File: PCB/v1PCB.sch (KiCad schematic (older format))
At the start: 218 parts, among them SW1 SW_PUSH, SW2 SW_PUSH, U1 STM32F072CBUx, U2 MCP1700-3302E_SOT23

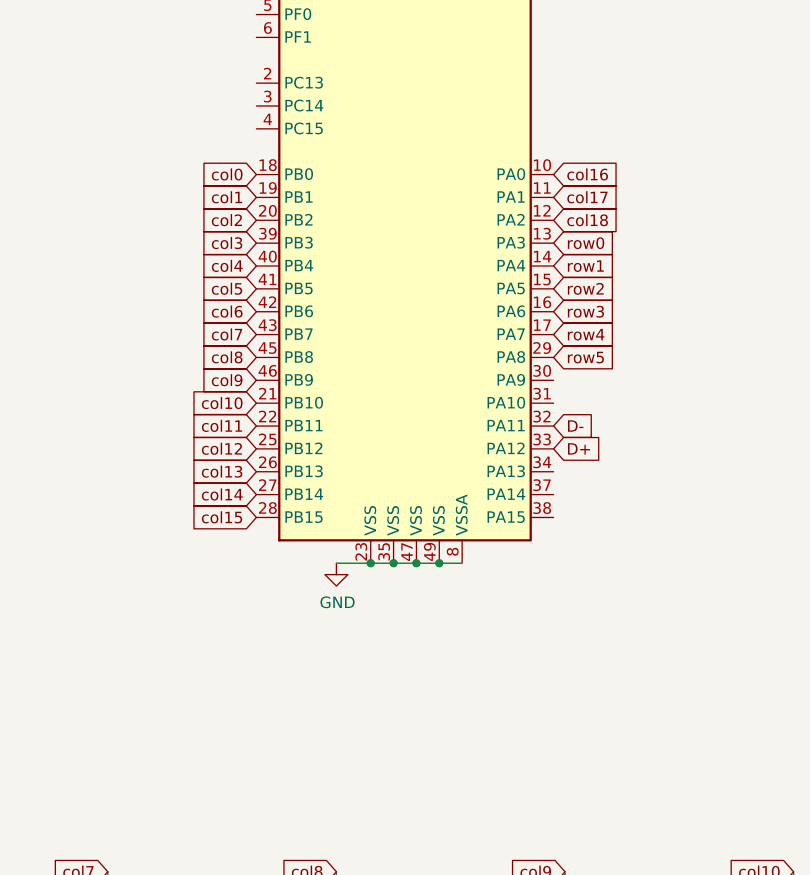
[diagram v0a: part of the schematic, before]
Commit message: Fixed a few runs, still need to add USB and redo VDDIO decoupling capacitors
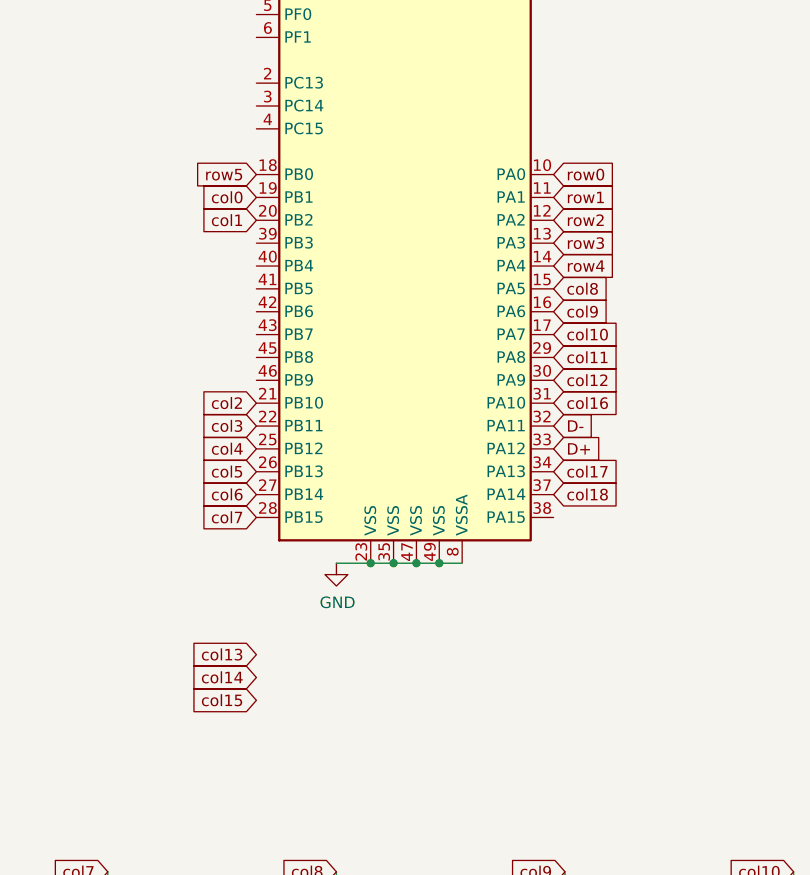
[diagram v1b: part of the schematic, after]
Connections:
- net col0: now also U1.19 (PB1); no longer U1.18 (PB0)
- net col1: now also U1.20 (PB2); no longer U1.19 (PB1)
- net col10: now also U1.17 (PA7); no longer U1.21 (PB10)
- net col11: now also U1.29 (PA8); no longer U1.22 (PB11)
- net col12: now also U1.30 (PA9); no longer U1.25 (PB12)
- net col13: no longer U1.26 (PB13)
- net col14: no longer U1.27 (PB14)
- net col15: no longer U1.28 (PB15)
- net col16: now also U1.31 (PA10); no longer U1.10 (PA0)
- net col17: now also U1.34 (PA13); no longer U1.11 (PA1)
- net col18: now also U1.37 (PA14); no longer U1.12 (PA2)
- net col2: now also U1.21 (PB10); no longer U1.20 (PB2)
- net col3: now also U1.22 (PB11); no longer U1.39 (PB3)
- net col4: now also U1.25 (PB12); no longer U1.40 (PB4)
- net col5: now also U1.26 (PB13); no longer U1.41 (PB5)
- net col6: now also U1.27 (PB14); no longer U1.42 (PB6)
- net col7: now also U1.28 (PB15); no longer U1.43 (PB7)
- net col8: now also U1.15 (PA5); no longer U1.45 (PB8)
- net col9: now also U1.16 (PA6); no longer U1.46 (PB9)
- net row0: now also U1.10 (PA0); no longer U1.13 (PA3)
- net row1: now also U1.11 (PA1); no longer U1.14 (PA4)
- net row2: now also U1.12 (PA2); no longer U1.15 (PA5)
- net row3: now also U1.13 (PA3); no longer U1.16 (PA6)
- net row4: now also U1.14 (PA4); no longer U1.17 (PA7)
- net row5: now also U1.18 (PB0); no longer U1.29 (PA8)
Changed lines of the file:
@@
 EESchema Schematic File Version 4
+LIBS:v1PCB-cache
 EELAYER 30 0
 EELAYER END
@@
 	20850 5750 20850 6750
 $Comp
-L MCU_ST_STM32F0:STM32F072CBUx U1
-U 1 1 5F25C889
-P 11200 2600
-F 0 "U1" H 11150 4281 50  0000 C CNN
-F 1 "STM32F072CBUx" H 11150 4190 50  0000 C CNN
-F 2 "Package_DFN_QFN:QFN-48-1EP_7x7mm_P0.5mm_EP5.6x5.6mm" H 10600 1200 50  0001 R CNN
-F 3 "http://www.st.com/st-web-ui/static/active/en/resource/technical/document/datasheet/DM00090510.pdf" H 11200 2600 50  0001 C CNN
-	1    11200 2600
-	1    0    0    -1
-$EndComp
-$Comp
 L Regulator_Linear:MCP1700-3302E_SOT23 U2
 U 1 1 5F2612C5
@@
 Wire Wire Line
 	13950 2000 13950 2150
-Connection ~ 11100 1100
-Connection ~ 11200 1100
-Connection ~ 11300 1100
-Connection ~ 11400 1100
 $Comp
 L power:+3.3V #PWR0104
@@
 Text GLabel 11800 3600 2    50   Input ~ 0
 D+
-Connection ~ 11000 4100
-Wire Wire Line
-	11000 4100 10850 4100
-Connection ~ 11100 4100
-Connection ~ 11200 4100
-Connection ~ 11300 4100
 $Comp
 L Device:R_Small R1
@@
 Wire Wire Line
 	6250 2200 6500 2200
-Wire Wire Line
-	11400 4100 11300 4100
-Wire Wire Line
-	11300 4100 11200 4100
-Wire Wire Line
-	11200 4100 11100 4100
-Wire Wire Line
-	11100 4100 11000 4100
-Wire Wire Line
-	11400 1100 11550 1100
-Wire Wire Line
-	11300 1100 11400 1100
-Wire Wire Line
-	11200 1100 11300 1100
-Wire Wire Line
-	11100 1100 11200 1100
-Wire Wire Line
-	11000 1100 11100 1100
-Text GLabel 11800 2700 2    50   Input ~ 0
-row0
-Text GLabel 11800 2800 2    50   Input ~ 0
-row1
-Text GLabel 11800 2900 2    50   Input ~ 0
-row2
-Text GLabel 11800 3000 2    50   Input ~ 0
-row3
-Text GLabel 11800 3100 2    50   Input ~ 0
-row4
-Text GLabel 11800 3200 2    50   Input ~ 0
-row5
-Text GLabel 10500 2500 0    50   Input ~ 0
-col1
-Text GLabel 10500 2400 0    50   Input ~ 0
-col0
-Text GLabel 10500 2600 0    50   Input ~ 0
-col2
-Text GLabel 10500 2700 0    50   Input ~ 0
-col3
-Text GLabel 10500 2800 0    50   Input ~ 0
-col4
-Text GLabel 10500 2900 0    50   Input ~ 0
-col5
-Text GLabel 10500 3000 0    50   Input ~ 0
-col6
-Text GLabel 10500 3100 0    50   Input ~ 0
-col7
-Text GLabel 10500 3200 0    50   Input ~ 0
-col8
-Text GLabel 10500 3300 0    50   Input ~ 0
-col9
-Text GLabel 10500 3400 0    50   Input ~ 0
-col10
-Text GLabel 10500 3500 0    50   Input ~ 0
-col11
-Text GLabel 10500 3600 0    50   Input ~ 0
-col12
-Text GLabel 10500 3700 0    50   Input ~ 0
-col13
-Text GLabel 10500 3800 0    50   Input ~ 0
-col14
-Text GLabel 10500 3900 0    50   Input ~ 0
-col15
-Text GLabel 11800 2400 2    50   Input ~ 0
+Text GLabel 11800 3400 2    50   Input ~ 0
 col16
-Text GLabel 11800 2500 2    50   Input ~ 0
+Text GLabel 11800 3700 2    50   Input ~ 0
 col17
-Text GLabel 11800 2600 2    50   Input ~ 0
+Text GLabel 11800 3800 2    50   Input ~ 0
 col18
 $Comp
@@
 $EndComp
 Connection ~ 6500 2200
+Text GLabel 11800 2800 2    50   Input ~ 0
+row4
+Text GLabel 11800 2700 2    50   Input ~ 0
+row3
+Text GLabel 11800 2600 2    50   Input ~ 0
+row2
+Text GLabel 11800 2500 2    50   Input ~ 0
+row1
+Text GLabel 11800 2400 2    50   Input ~ 0
+row0
+Text GLabel 10500 3500 0    50   Input ~ 0
+col3
+Text GLabel 10500 3600 0    50   Input ~ 0
+col4
+Text GLabel 10500 3700 0    50   Input ~ 0
+col5
+Text GLabel 10500 3800 0    50   Input ~ 0
+col6
+Text GLabel 10500 3900 0    50   Input ~ 0
+col7
+Text GLabel 11800 3000 2    50   Input ~ 0
+col9
+Text GLabel 11800 3100 2    50   Input ~ 0
+col10
+Text GLabel 11800 3300 2    50   Input ~ 0
+col12
+Text GLabel 10500 4500 0    50   Input ~ 0
+col13
+Text GLabel 10500 4600 0    50   Input ~ 0
+col14
+Text GLabel 10500 4700 0    50   Input ~ 0
+col15
+Text GLabel 10500 3400 0    50   Input ~ 0
+col2
+Connection ~ 11100 1100
+Connection ~ 11200 1100
+Connection ~ 11300 1100
+Connection ~ 11400 1100
+Connection ~ 11000 4100
+Wire Wire Line
+	11000 4100 10850 4100
+Wire Wire Line
+	11100 4100 11000 4100
+Connection ~ 11100 4100
+Connection ~ 11200 4100
+Connection ~ 11300 4100
+Wire Wire Line
+	11000 1100 11100 1100
+Wire Wire Line
+	11400 4100 11300 4100
+Wire Wire Line
+	11300 1100 11400 1100
+Wire Wire Line
+	11300 4100 11200 4100
+Wire Wire Line
+	11200 1100 11300 1100
+Wire Wire Line
+	11200 4100 11100 4100
+Wire Wire Line
+	11100 1100 11200 1100
+Wire Wire Line
+	11400 1100 11550 1100
+Text GLabel 11800 2900 2    50   Input ~ 0
+col8
+$Comp
+L MCU_ST_STM32F0:STM32F072CBUx U1
+U 1 1 5F25C889
+P 11200 2600
+F 0 "U1" H 11150 4281 50  0000 C CNN
+F 1 "STM32F072CBUx" H 11150 4190 50  0000 C CNN
+F 2 "Package_DFN_QFN:QFN-48-1EP_7x7mm_P0.5mm_EP5.6x5.6mm" H 10600 1200 50  0001 R CNN
+F 3 "http://www.st.com/st-web-ui/static/active/en/resource/technical/document/datasheet/DM00090510.pdf" H 11200 2600 50  0001 C CNN
+	1    11200 2600
+	1    0    0    -1
+$EndComp
+Text GLabel 11800 3200 2    50   Input ~ 0
+col11
+Text GLabel 10500 2500 0    50   Input ~ 0
+col0
+Text GLabel 10500 2600 0    50   Input ~ 0
+col1
+Text GLabel 10500 2400 0    50   Input ~ 0
+row5
 $EndSCHEMATC

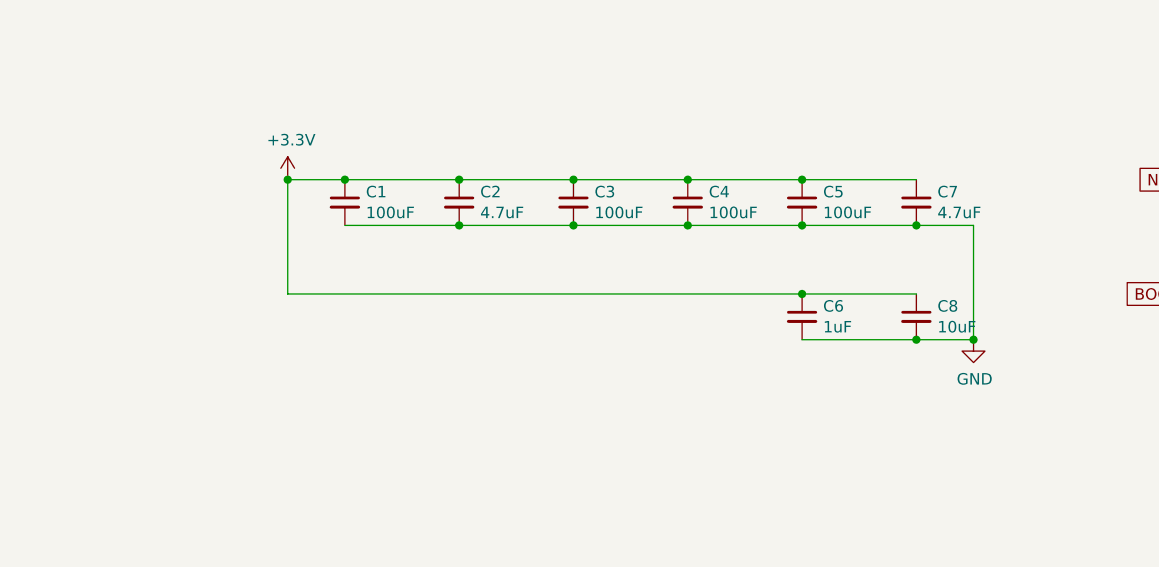
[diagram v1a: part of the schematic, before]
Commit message: Almost done with cap placement, still neeed to add USBC
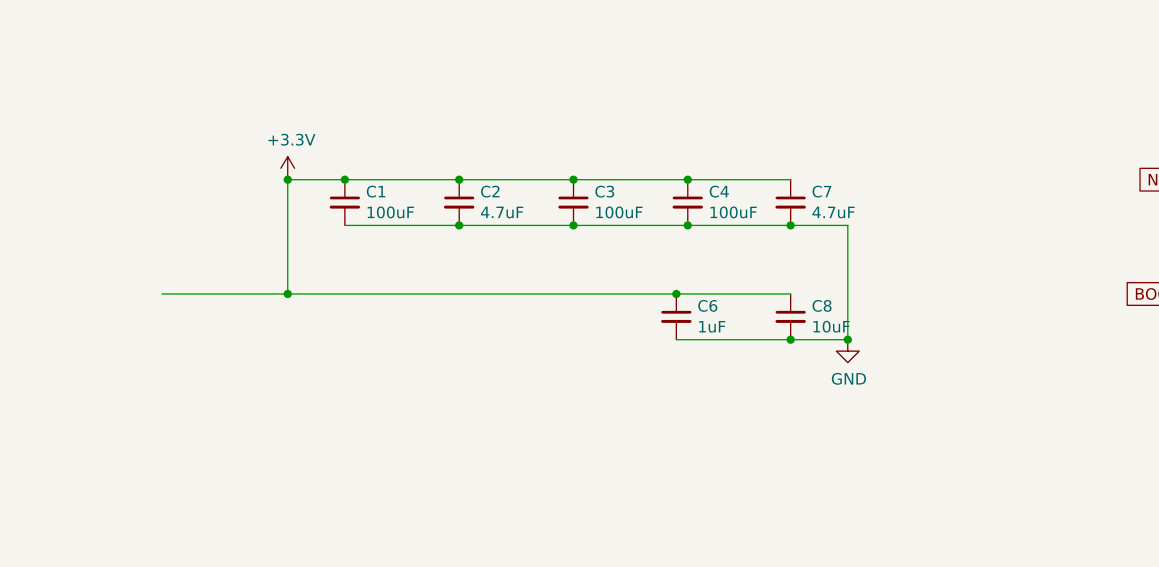
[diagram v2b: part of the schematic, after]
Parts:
- removed C5: 100uF, Capacitor_SMD:C_0805_2012Metric, symbol Device:C_Small
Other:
- moved on the sheet: C6, C7, C8
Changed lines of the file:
@@
-$EndComp
-$Comp
-L Device:C_Small C5
-U 1 1 5F5943AB
-P 5750 1600
-F 0 "C5" H 5842 1646 50  0000 L CNN
-F 1 "100uF" H 5842 1555 50  0000 L CNN
-F 2 "Capacitor_SMD:C_0805_2012Metric" H 5750 1600 50  0001 C CNN
-F 3 "~" H 5750 1600 50  0001 C CNN
-	1    5750 1600
-	1    0    0    -1
-$EndComp
-$Comp
-L Device:C_Small C7
-U 1 1 5F59495C
-P 6250 1600
-F 0 "C7" H 6342 1646 50  0000 L CNN
-F 1 "4.7uF" H 6342 1555 50  0000 L CNN
-F 2 "Capacitor_SMD:C_0805_2012Metric" H 6250 1600 50  0001 C CNN
-F 3 "~" H 6250 1600 50  0001 C CNN
-	1    6250 1600
-	1    0    0    -1
 $EndComp
 $Comp
 L Device:C_Small C6
 U 1 1 5F5950B7
-P 5750 2100
-F 0 "C6" H 5842 2146 50  0000 L CNN
-F 1 "1uF" H 5842 2055 50  0000 L CNN
-F 2 "Capacitor_SMD:C_0805_2012Metric" H 5750 2100 50  0001 C CNN
-F 3 "~" H 5750 2100 50  0001 C CNN
-	1    5750 2100
-	1    0    0    -1
-$EndComp
-$Comp
-L Device:C_Small C8
-U 1 1 5F5957F8
-P 6250 2100
-F 0 "C8" H 6342 2146 50  0000 L CNN
-F 1 "10uF" H 6342 2055 50  0000 L CNN
-F 2 "Capacitor_SMD:C_0805_2012Metric" H 6250 2100 50  0001 C CNN
-F 3 "~" H 6250 2100 50  0001 C CNN
-	1    6250 2100
+P 5200 2100
+F 0 "C6" H 5292 2146 50  0000 L CNN
+F 1 "1uF" H 5292 2055 50  0000 L CNN
+F 2 "Capacitor_SMD:C_0805_2012Metric" H 5200 2100 50  0001 C CNN
+F 3 "~" H 5200 2100 50  0001 C CNN
+	1    5200 2100
 	1    0    0    -1
 $EndComp
@@
 Wire Wire Line
 	4750 1500 5250 1500
-Connection ~ 5250 1500
-Wire Wire Line
-	5250 1500 5750 1500
-Connection ~ 5750 1500
-Wire Wire Line
-	5750 1500 6250 1500
 Wire Wire Line
 	3750 1700 4250 1700
-Wire Wire Line
-	6500 1700 6500 2200
 Connection ~ 4250 1700
 Wire Wire Line
@@
 Wire Wire Line
 	4750 1700 5250 1700
-Connection ~ 5250 1700
-Wire Wire Line
-	5250 1700 5750 1700
-Connection ~ 5750 1700
-Wire Wire Line
-	5750 1700 6250 1700
-Connection ~ 6250 1700
-Wire Wire Line
-	6250 1700 6500 1700
 Wire Wire Line
 	3500 1500 3500 2000
 Wire Wire Line
-	3500 2000 5750 2000
+	2950 2000 3500 2000
 Connection ~ 3500 1500
-Connection ~ 5750 2000
-Wire Wire Line
-	5750 2000 6250 2000
-Wire Wire Line
-	5750 2200 6250 2200
-Connection ~ 6250 2200
-Wire Wire Line
-	6250 2200 6500 2200
 Text GLabel 11800 3400 2    50   Input ~ 0
 col16
@@
 col18
 $Comp
-L power:GND #PWR?
+L power:GND #PWR0101
 U 1 1 5F81C895
 P 13950 2150
-F 0 "#PWR?" H 13950 1900 50  0001 C CNN
+F 0 "#PWR0101" H 13950 1900 50  0001 C CNN
 F 1 "GND" H 13955 1977 50  0000 C CNN
 F 2 "" H 13950 2150 50  0001 C CNN
@@
 $EndComp
 $Comp
-L power:GND #PWR?
+L power:GND #PWR0105
 U 1 1 5F81E65E
 P 10850 4100
-F 0 "#PWR?" H 10850 3850 50  0001 C CNN
+F 0 "#PWR0105" H 10850 3850 50  0001 C CNN
 F 1 "GND" H 10855 3927 50  0000 C CNN
 F 2 "" H 10850 4100 50  0001 C CNN
@@
 $EndComp
 $Comp
-L power:GND #PWR?
+L power:GND #PWR0106
 U 1 1 5F81EFCA
 P 7750 2500
-F 0 "#PWR?" H 7750 2250 50  0001 C CNN
+F 0 "#PWR0106" H 7750 2250 50  0001 C CNN
 F 1 "GND" H 7755 2327 50  0000 C CNN
 F 2 "" H 7750 2500 50  0001 C CNN
@@
 $EndComp
 $Comp
-L power:GND #PWR?
+L power:GND #PWR0109
 U 1 1 5F820883
 P 8750 1500
-F 0 "#PWR?" H 8750 1250 50  0001 C CNN
+F 0 "#PWR0109" H 8750 1250 50  0001 C CNN
 F 1 "GND" H 8755 1327 50  0000 C CNN
 F 2 "" H 8750 1500 50  0001 C CNN
@@
 	1    0    0    -1
 $EndComp
-$Comp
-L power:GND #PWR?
-U 1 1 5F820EC9
-P 6500 2200
-F 0 "#PWR?" H 6500 1950 50  0001 C CNN
-F 1 "GND" H 6505 2027 50  0000 C CNN
-F 2 "" H 6500 2200 50  0001 C CNN
-F 3 "" H 6500 2200 50  0001 C CNN
-	1    6500 2200
-	1    0    0    -1
-$EndComp
-Connection ~ 6500 2200
 Text GLabel 11800 2800 2    50   Input ~ 0
 row4
@@
 Text GLabel 10500 2400 0    50   Input ~ 0
 row5
+Connection ~ 5200 2000
+Connection ~ 5950 2200
+$Comp
+L power:GND #PWR0111
+U 1 1 5F820EC9
+P 5950 2200
+F 0 "#PWR0111" H 5950 1950 50  0001 C CNN
+F 1 "GND" H 5955 2027 50  0000 C CNN
+F 2 "" H 5950 2200 50  0001 C CNN
+F 3 "" H 5950 2200 50  0001 C CNN
+	1    5950 2200
+	1    0    0    -1
+$EndComp
+Wire Wire Line
+	5700 2200 5950 2200
+Connection ~ 5700 2200
+Wire Wire Line
+	5200 2200 5700 2200
+Wire Wire Line
+	5200 2000 5700 2000
+Wire Wire Line
+	5700 1700 5950 1700
+Wire Wire Line
+	5950 1700 5950 2200
+$Comp
+L Device:C_Small C8
+U 1 1 5F5957F8
+P 5700 2100
+F 0 "C8" H 5792 2146 50  0000 L CNN
+F 1 "10uF" H 5792 2055 50  0000 L CNN
+F 2 "Capacitor_SMD:C_0805_2012Metric" H 5700 2100 50  0001 C CNN
+F 3 "~" H 5700 2100 50  0001 C CNN
+	1    5700 2100
+	1    0    0    -1
+$EndComp
+$Comp
+L Device:C_Small C7
+U 1 1 5F59495C
+P 5700 1600
+F 0 "C7" H 5792 1646 50  0000 L CNN
+F 1 "4.7uF" H 5792 1555 50  0000 L CNN
+F 2 "Capacitor_SMD:C_0805_2012Metric" H 5700 1600 50  0001 C CNN
+F 3 "~" H 5700 1600 50  0001 C CNN
+	1    5700 1600
+	1    0    0    -1
+$EndComp
+Connection ~ 3500 2000
+Wire Wire Line
+	3500 2000 5200 2000
+Wire Wire Line
+	5250 1500 5700 1500
+Connection ~ 5250 1500
+Wire Wire Line
+	5700 1700 5250 1700
+Connection ~ 5700 1700
+Connection ~ 5250 1700
 $EndSCHEMATC

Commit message: Finished schematic, begin drawing traces
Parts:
- added C5: 4.7nF, Capacitor_SMD:C_0603_1608Metric, symbol Device:C_Small
- added F1: Polyfuse (1A), Fuse:Fuse_1206_3216Metric, symbol Device:Polyfuse_Small
- added R3: 1M, Resistor_SMD:R_0805_2012Metric, symbol Device:R_Small
- added R4, R5: 5.1k, Resistor_SMD:R_0805_2012Metric, symbol Device:R_Small
- added USB1: HRO-TYPE-C-31-M-12, Type-C:HRO-TYPE-C-31-M-12-Assembly, symbol Type-C:HRO-TYPE-C-31-M-12
- C1, C3, C4: value 100uF -> 100nF; footprint Capacitor_SMD:C_0805_2012Metric -> Capacitor_SMD:C_0402_1005Metric
- C10, C9: footprint Capacitor_SMD:C_0805_2012Metric -> Capacitor_SMD:C_0402_1005Metric
- C2, C6, C7: footprint Capacitor_SMD:C_0805_2012Metric -> Capacitor_SMD:C_0603_1608Metric
- C8: value 10uF -> 10nF; footprint Capacitor_SMD:C_0805_2012Metric -> Capacitor_SMD:C_0402_1005Metric
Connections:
- net +5V: now also F1.2
- net D+: now also USB1.6 (DP1), USB1.8 (DP2)
- net D-: now also USB1.5 (DN2), USB1.7 (DN1)
- net GND: now also C5.1, R3.1, R4.1, R5.1, USB1.1 (GND), USB1.12 (GND)
- net col0: no longer U1.19 (PB1)
- net col1: no longer U1.20 (PB2)
- net col10: no longer U1.17 (PA7)
- net col11: no longer U1.29 (PA8)
- net col12: no longer U1.30 (PA9)
- net col16: no longer U1.31 (PA10)
- net col17: no longer U1.34 (PA13)
- net col18: no longer U1.37 (PA14)
- net col2: no longer U1.21 (PB10)
- net col3: no longer U1.22 (PB11)
- net col4: no longer U1.25 (PB12)
- net col5: no longer U1.26 (PB13)
- net col6: no longer U1.27 (PB14)
- net col7: no longer U1.28 (PB15)
- net col8: no longer U1.15 (PA5)
- net col9: no longer U1.16 (PA6)
- net row0: no longer U1.10 (PA0)
- net row1: no longer U1.11 (PA1)
- net row2: no longer U1.12 (PA2)
- net row3: no longer U1.13 (PA3)
- net row4: no longer U1.14 (PA4)
- net row5: no longer U1.18 (PB0)
- new net: R5.2, USB1.10 (CC2)
- new net: F1.1, USB1.11 (VBUS), USB1.2 (VBUS)
- new net: C5.2, R3.2, USB1.13 (SHIELD)
- new net: R4.2, USB1.4 (CC1)

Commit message: Need to finish reset buttons, confirm routing of 3V3 and GND, review overall package
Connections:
- net col0: now also K_71.1 (COL), U1.42 (PB6)
- net col1: now also K_38.1 (COL), K_56.1 (COL), K_72.1 (COL), U1.41 (PB5); no longer K_71.1 (COL)
- net col10: now also K_47.1 (COL), K_65.1 (COL), K_81.1 (COL), U1.26 (PB13); no longer K_46.1 (COL), K_64.1 (COL), K_80.1 (COL)
- net col11: now also K_48.1 (COL), K_66.1 (COL), U1.25 (PB12); no longer K_47.1 (COL), K_65.1 (COL), K_81.1 (COL)
- net col12: now also K_49.1 (COL), K_82.1 (COL), U1.22 (PB11); no longer K_48.1 (COL), K_66.1 (COL)
- net col13: now also K_32.1 (COL), U1.21 (PB10); no longer K_49.1 (COL), K_82.1 (COL)
- net col14: now also U1.20 (PB2); no longer K_32.1 (COL)
- net col15: now also U1.19 (PB1)
- net col16: now also U1.18 (PB0)
- net col17: now also U1.17 (PA7)
- net col18: now also U1.16 (PA6)
- net col2: now also K_39.1 (COL), K_57.1 (COL), K_73.1 (COL), U1.40 (PB4); no longer K_38.1 (COL), K_56.1 (COL), K_72.1 (COL)
- net col3: now also K_40.1 (COL), K_58.1 (COL), K_74.1 (COL), U1.39 (PB3); no longer K_39.1 (COL), K_57.1 (COL), K_73.1 (COL)
- net col4: now also K_41.1 (COL), K_59.1 (COL), K_75.1 (COL), U1.38 (PA15); no longer K_40.1 (COL), K_58.1 (COL), K_74.1 (COL)
- net col5: now also K_42.1 (COL), K_60.1 (COL), K_76.1 (COL), U1.37 (PA14); no longer K_41.1 (COL), K_59.1 (COL), K_75.1 (COL)
- net col6: now also K_43.1 (COL), K_61.1 (COL), K_77.1 (COL), U1.30 (PA9); no longer K_42.1 (COL), K_60.1 (COL), K_76.1 (COL)
- net col7: now also K_44.1 (COL), K_62.1 (COL), K_78.1 (COL), U1.29 (PA8); no longer K_43.1 (COL), K_61.1 (COL), K_77.1 (COL)
- net col8: now also K_45.1 (COL), K_63.1 (COL), K_79.1 (COL), U1.28 (PB15); no longer K_44.1 (COL), K_62.1 (COL), K_78.1 (COL)
- net col9: now also K_46.1 (COL), K_64.1 (COL), K_80.1 (COL), U1.27 (PB14); no longer K_45.1 (COL), K_63.1 (COL), K_79.1 (COL)
- net row0: now also U1.10 (PA0)
- net row1: now also U1.11 (PA1)
- net row2: now also D_54.1 (K), U1.12 (PA2)
- net row3: now also U1.13 (PA3); no longer D_54.1 (K)
- net row4: now also D_87.1 (K), U1.14 (PA4)
- net row5: now also U1.15 (PA5); no longer D_87.1 (K)
